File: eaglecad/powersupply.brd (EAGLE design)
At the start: 82.5 x 100 mm, 10 parts

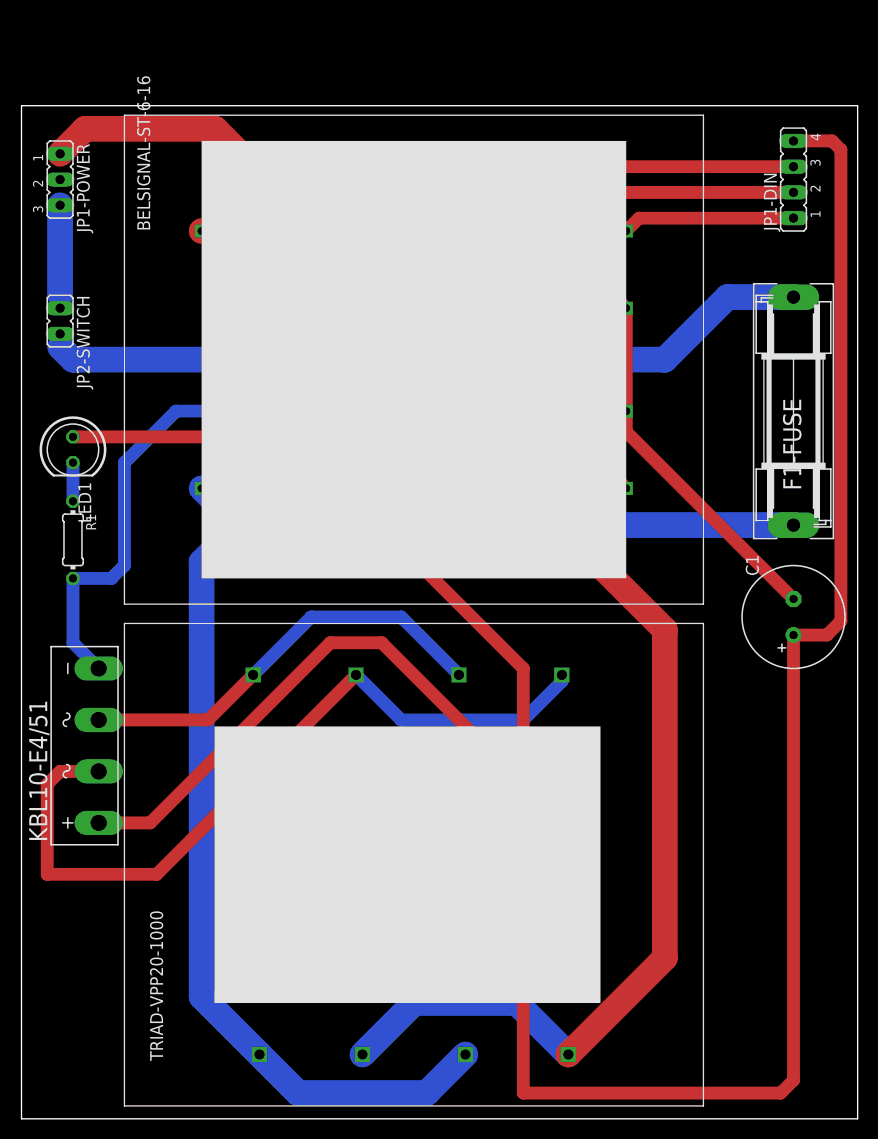
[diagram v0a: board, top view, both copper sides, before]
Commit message: changed orientation of fuse and switch on power supply board
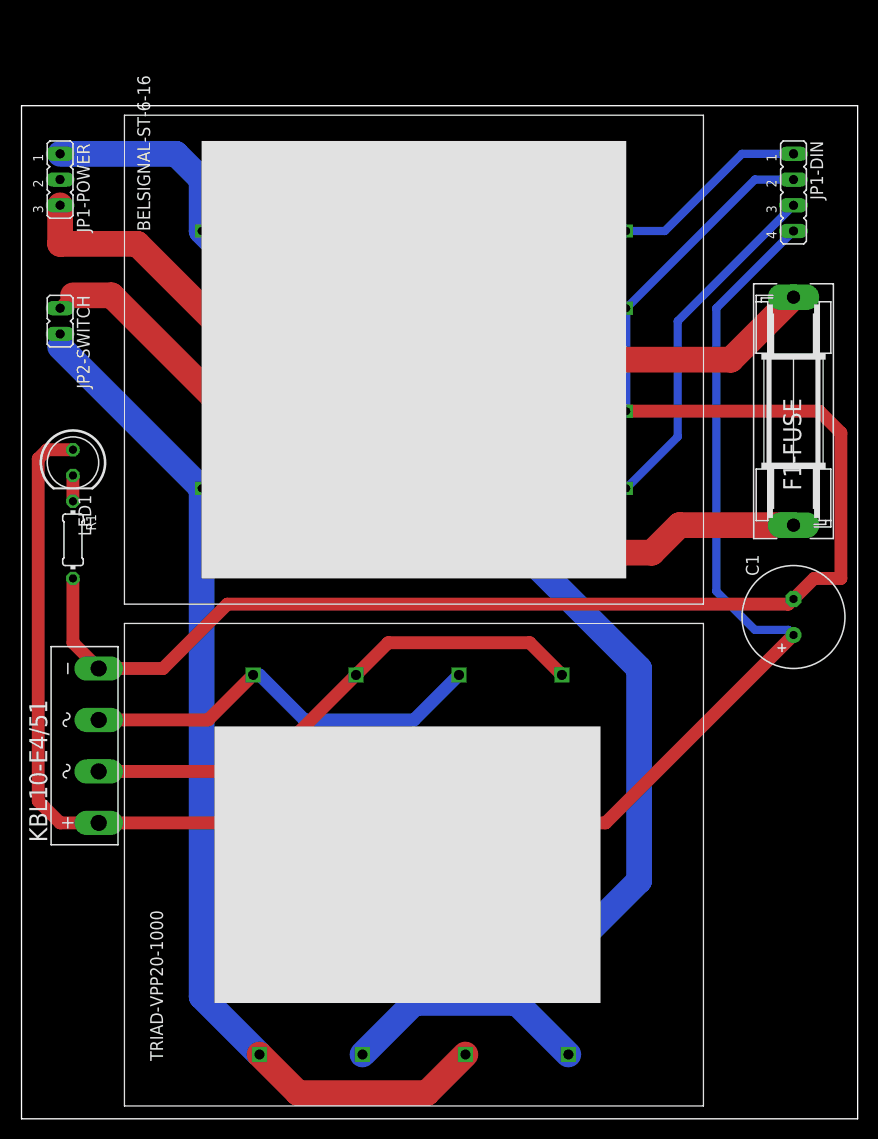
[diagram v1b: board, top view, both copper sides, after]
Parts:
- moved LED1 1.27 mm to (5.08, 64.8)
- moved JP1-DIN 1.27 mm to (76.2, 91.4), turned to 270 degrees
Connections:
- removed net AC-IN-1: JP1-POWER.3, JP2-SWITCH.1
- removed net AC-IN-1-AFTER-FUSE: BELSIGNAL-ST-6-16.P1, F1-FUSE.2, TRIAD-VPP20-1000.P1, TRIAD-VPP20-1000.P4
- removed net AC-IN-2-BEFORE-FUSE: F1-FUSE.1, JP2-SWITCH.2
- new net AC-IN-AFTER-FUSE: F1-FUSE.2, JP2-SWITCH.1
- new net AC-IN-AFTER-SW: BELSIGNAL-ST-6-16.P1, JP2-SWITCH.2, TRIAD-VPP20-1000.P1, TRIAD-VPP20-1000.P4
- new net AC-IN-BEFORE-FUSE: F1-FUSE.1, JP1-POWER.3
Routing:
- net AC-IN-1-AFTER-FUSE: track 139.5 -> 0.00 mm
- net DC-OUT: track 278.8 -> 168.8 mm
- net AC-IN-AFTER-SW: track 0.00 -> 102.8 mm
- net AC-IN-AFTER-FUSE: track 0.00 -> 84.6 mm
- net AC-IN-BEFORE-FUSE: track 0.00 -> 83.5 mm
- net AC-IN-2-BEFORE-FUSE: track 76.7 -> 0.00 mm
- net AC-FOR-RECT-A: track 77.5 -> 52.3 mm
- net AC2: track 57.5 -> 34.8 mm
- net AC-IN-2: track 160.9 -> 143.7 mm
- net AC-IN-1: track 10.2 -> 0.00 mm
- net GND: track 145.5 -> 155.3 mm
- net AC1: track 17.0 -> 19.7 mm
- net N$1: track 3.81 -> 2.54 mm
- net AC-FOR-RECT-B: track 42.1 -> 41.1 mm
